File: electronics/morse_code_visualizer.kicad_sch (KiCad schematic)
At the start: 10 parts, among them SW1 Push_Button

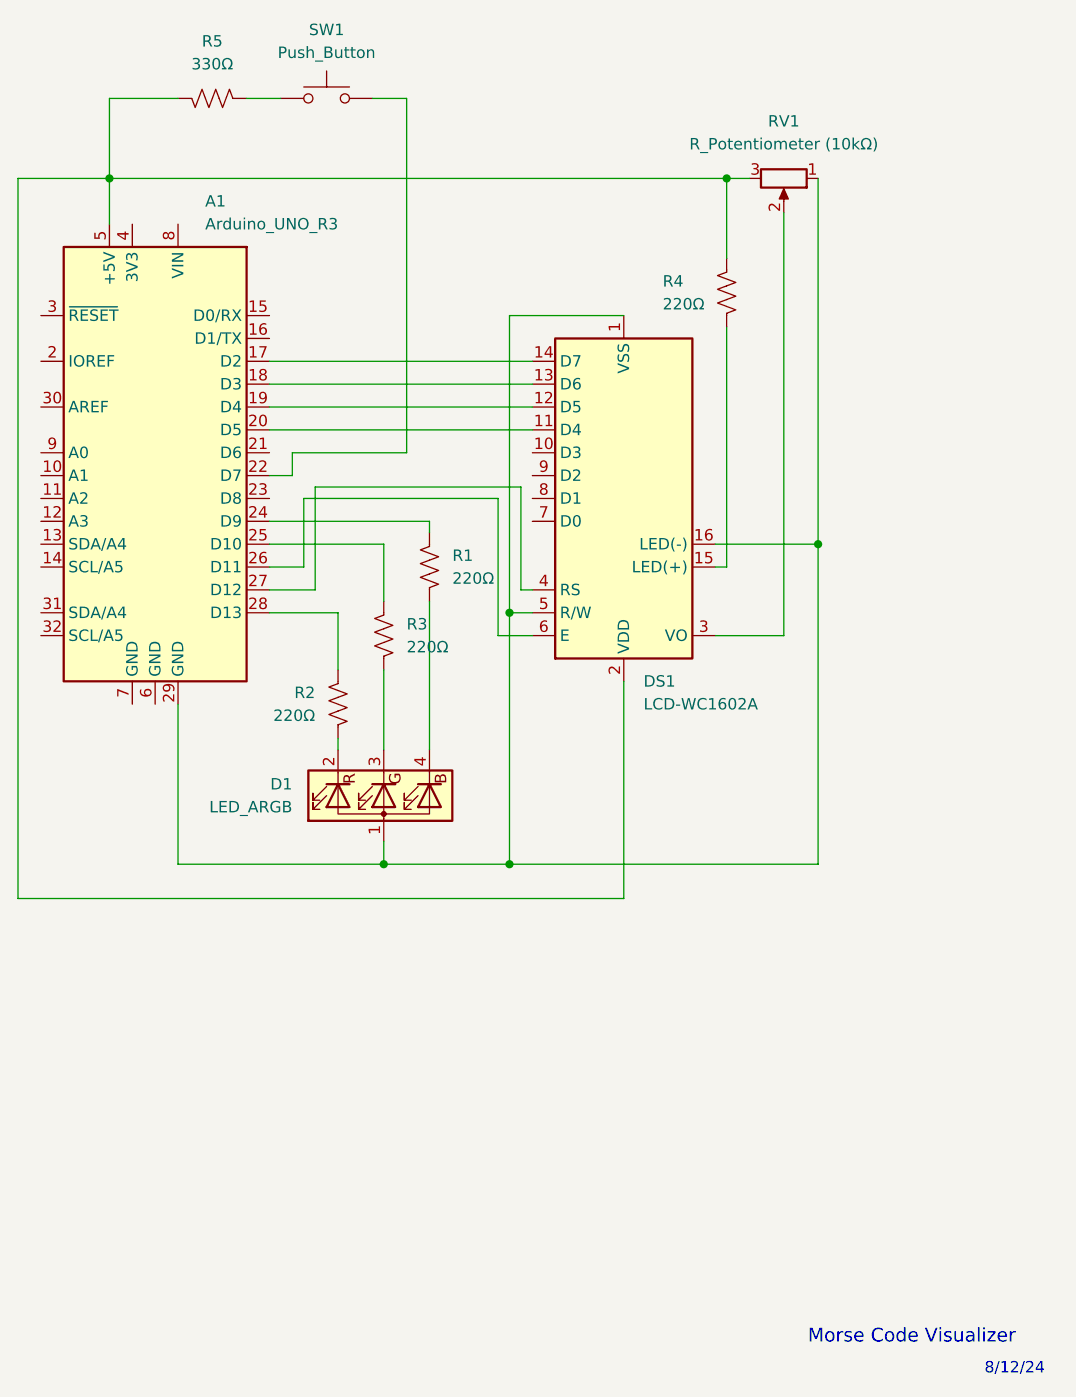
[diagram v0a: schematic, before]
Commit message: LCD Buffer & functions on main.cpp
- Added separate functions for checking the user's input as well as clearing it
- Adjusted the functions for setting the color as well as specific pin connections
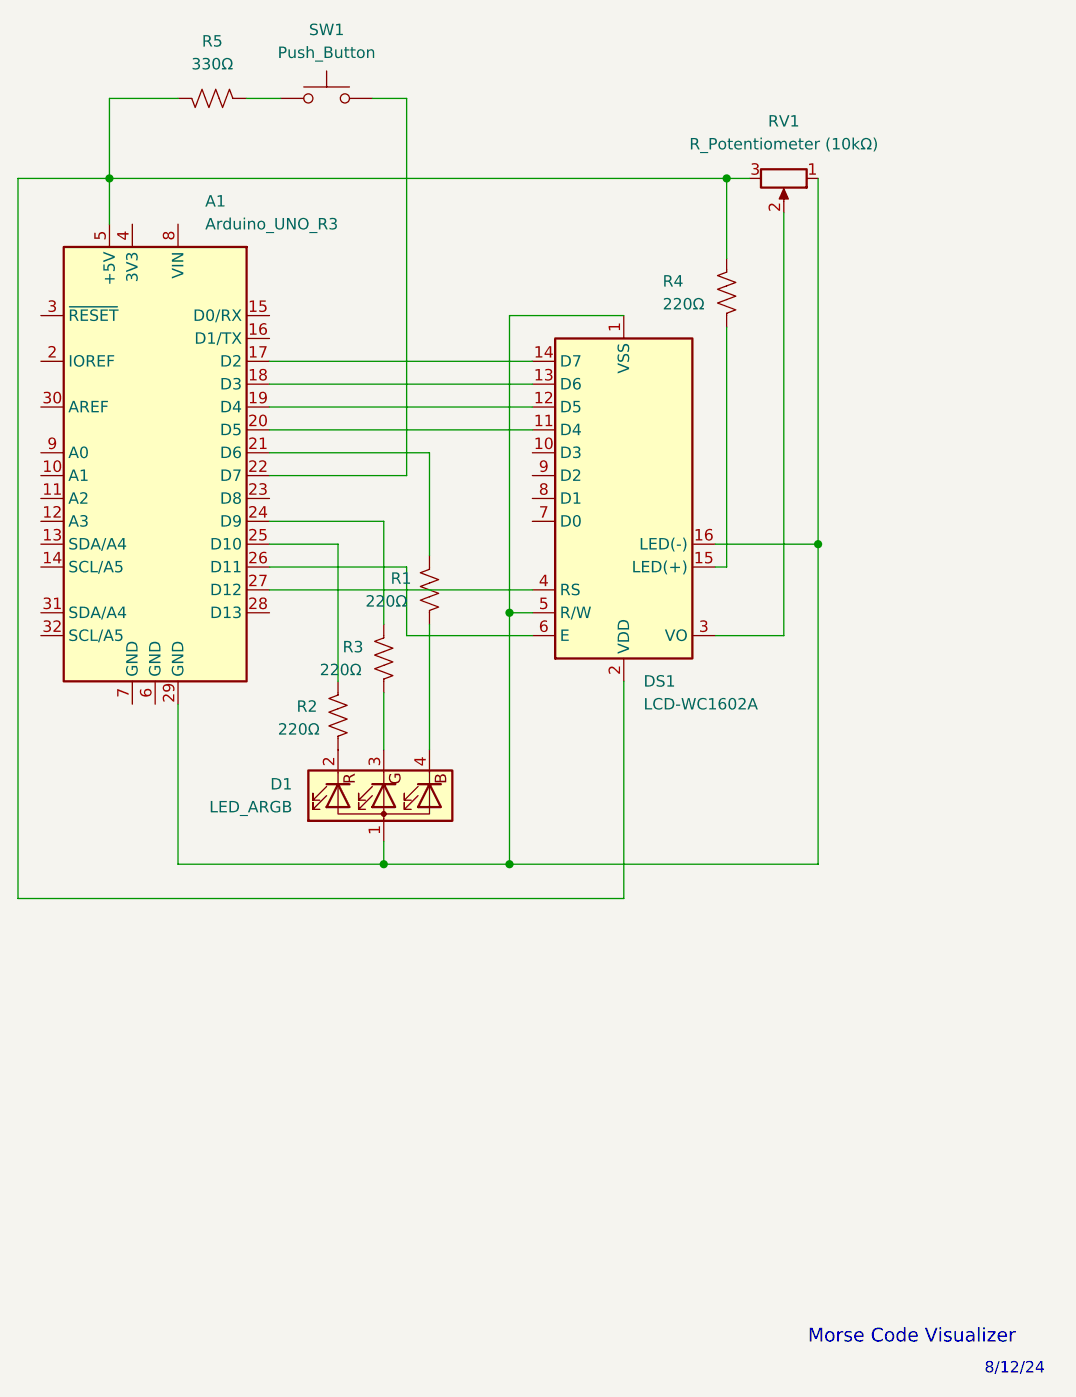
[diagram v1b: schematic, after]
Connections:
- net at A1.21 (D6): now also R1.1
- net at A1.24 (D9): now also R3.1; no longer R1.1
- net at A1.25 (D10): now also R2.1; no longer R3.1
- net at A1.28 (D13): no longer R2.1
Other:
- moved on the sheet: R1, R2, R3

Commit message: Updated schematic for electronics.
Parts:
- added D2: LED, symbol Device:LED
- added R6: R_US, symbol Device:R_US
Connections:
- net at A1.22 (D7), SW1.1: now also R6.1
- new net: D2.1 (K), R6.2
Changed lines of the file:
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@@
+	)
+	(junction
+		(at 143.51 52.07)
+		(diameter 0)
+		(color 0 0 0 0)
 	)
 	(junction
@@
 	(wire
 		(pts
+			(xy 154.94 52.07) (xy 160.02 52.07)
+		)
+		(stroke
+			(width 0)
+			(type default)
+		)
+	)
+	(wire
+		(pts
 			(xy 146.05 91.44) (xy 128.27 91.44)
 		)
@@
 			(type default)
 			(color 0 0 0 1)
+		)
+	)
+	(wire
+		(pts
+			(xy 143.51 52.07) (xy 147.32 52.07)
+		)
+		(stroke
+			(width 0)
+			(type default)
 		)
 	)
@@
 			(font
 				(size 1.524 1.524)
+			)
+		)
+	)
+	(symbol
+		(lib_id "Device:LED")
+		(at 163.83 52.07 0)
+		(unit 1)
+		(exclude_from_sim no)
+		(in_bom yes)
+		(on_board yes)
+		(dnp no)
+		(fields_autoplaced yes)
+		(property "Reference" "D2"
+			(at 162.2425 45.72 0)
+			(effects
+				(font
+					(size 1.27 1.27)
+				)
+			)
+		)
+		(property "Value" "LED"
+			(at 162.2425 48.26 0)
+			(effects
+				(font
+					(size 1.27 1.27)
+				)
+			)
+		)
+		(property "Footprint" ""
+			(at 163.83 52.07 0)
+			(effects
+				(font
+					(size 1.27 1.27)
+				)
+				(hide yes)
+			)
+		)
+		(property "Datasheet" "~"
+			(at 163.83 52.07 0)
+			(effects
+				(font
+					(size 1.27 1.27)
+				)
+				(hide yes)
+			)
+		)
+		(property "Description" "Light emitting diode"
+			(at 163.83 52.07 0)
+			(effects
+				(font
+					(size 1.27 1.27)
+				)
+				(hide yes)
+			)
+		)
+		(pin "2"
+		)
+		(pin "1"
+		)
+		(instances
+			(project ""
+				(path "/fec54f5b-1400-4a4b-bbab-423fb0ef72e0"
+					(reference "D2")
+					(unit 1)
+				)
 			)
 		)
@@
 					(unit 1)
 				)
+			)
+		)
+	)
+	(symbol
+		(lib_id "Device:R_US")
+		(at 151.13 52.07 90)
+		(unit 1)
+		(exclude_from_sim no)
+		(in_bom yes)
+		(on_board yes)
+		(dnp no)
+		(fields_autoplaced yes)
+		(property "Reference" "R6"
+			(at 151.13 45.72 90)
+			(effects
+				(font
+					(size 1.27 1.27)
+				)
+			)
+		)
+		(property "Value" "R_US"
+			(at 151.13 48.26 90)
+			(effects
+				(font
+					(size 1.27 1.27)
+				)
+			)
+		)
+		(property "Footprint" ""
+			(at 151.384 51.054 90)
+			(effects
+				(font
+					(size 1.27 1.27)
+				)
+				(hide yes)
+			)
+		)
+		(property "Datasheet" "~"
+			(at 151.13 52.07 0)
+			(effects
+				(font
+					(size 1.27 1.27)
+				)
+				(hide yes)
+			)
+		)
+		(property "Description" "Resistor, US symbol"
+			(at 151.13 52.07 0)
+			(effects
+				(font
+					(size 1.27 1.27)
+				)
+				(hide yes)
+			)
+		)
+		(pin "1"
+		)
+		(pin "2"
+		)
+		(instances
+			(project ""
+				(path "/fec54f5b-1400-4a4b-bbab-423fb0ef72e0"
+					(reference "R6")
+					(unit 1)
+				)

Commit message: Updated schematic
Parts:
- R6: value R_US -> 330Ω
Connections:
- net at D2.1 (K), R6.2: now also A1.22 (D7)
- net at D2.2 (A): now also A1.29 (GND), D1.1 (A), DS1.1 (VSS), DS1.16 (LED(-)), DS1.5 (R/W), RV1.1
- net at R6.1, SW1.1: no longer A1.22 (D7)
